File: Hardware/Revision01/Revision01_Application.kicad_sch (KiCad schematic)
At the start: 25 parts, among them J2 Conn_02x08_Odd_Even, J3 Conn_01x04, J4 Conn_02x08_Odd_Even, Q2 PMV32UP,215, Q3 PMV32UP,215, U2 MRF89XAM9AT-I/RM, U4 ICM-45605

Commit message: added back powerflags back for ERC
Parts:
- J2, J4: footprint (none) -> Connector_PinHeader_2.54mm:PinHeader_2x08_P2.54mm_Vertical
- J3: footprint (none) -> Connector_PinHeader_2.54mm:PinHeader_1x04_P2.54mm_Vertical
- U2: footprint MOD_MRF89XAM9A_MCH -> MRF89XAM9AT-antenna:MOD_MRF89XAM9A_MCH
- U4: footprint ICM-45605:XDCR_ICM-45605 -> ICM-45605-gyroscope:XDCR_ICM-45605
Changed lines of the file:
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@@
 			)
 		)
-		(property "Footprint" ""
+		(property "Footprint" "Connector_PinHeader_2.54mm:PinHeader_2x08_P2.54mm_Vertical"
 			(at 127 30.48 0)
 			(effects
@@
 			)
 		)
-		(property "Footprint" ""
+		(property "Footprint" "Connector_PinHeader_2.54mm:PinHeader_2x08_P2.54mm_Vertical"
 			(at 152.4 29.21 0)
 			(effects
@@
 			)
 		)
-		(property "Footprint" ""
+		(property "Footprint" "Connector_PinHeader_2.54mm:PinHeader_1x04_P2.54mm_Vertical"
 			(at 147.32 105.41 0)
 			(effects
@@
 			)
 		)
-		(property "Footprint" "MOD_MRF89XAM9A_MCH"
+		(property "Footprint" "MRF89XAM9AT-antenna:MOD_MRF89XAM9A_MCH"
 			(at 194.31 29.21 0)
 			(effects
@@
 			)
 		)
-		(property "Footprint" "ICM-45605:XDCR_ICM-45605"
+		(property "Footprint" "ICM-45605-gyroscope:XDCR_ICM-45605"
 			(at 231.14 88.9 0)
 			(effects

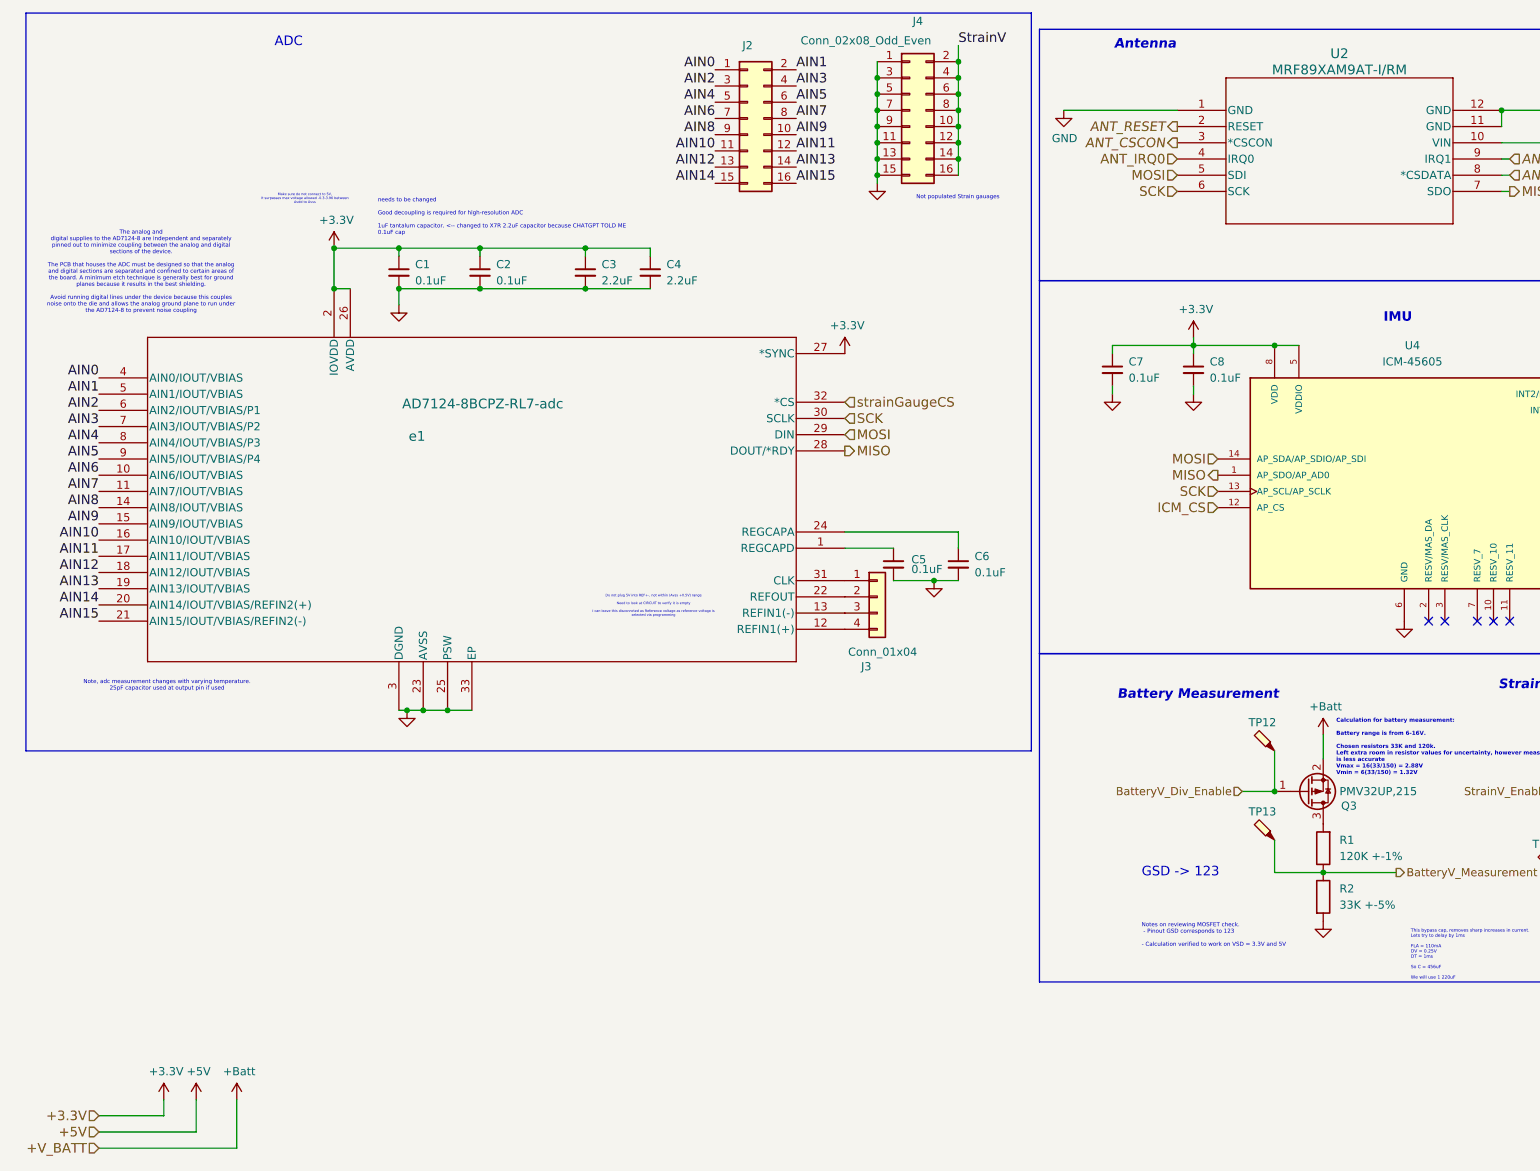
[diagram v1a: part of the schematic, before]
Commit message: added netclasses again changed power to be globally used strain gauges symbol created and added to schematic
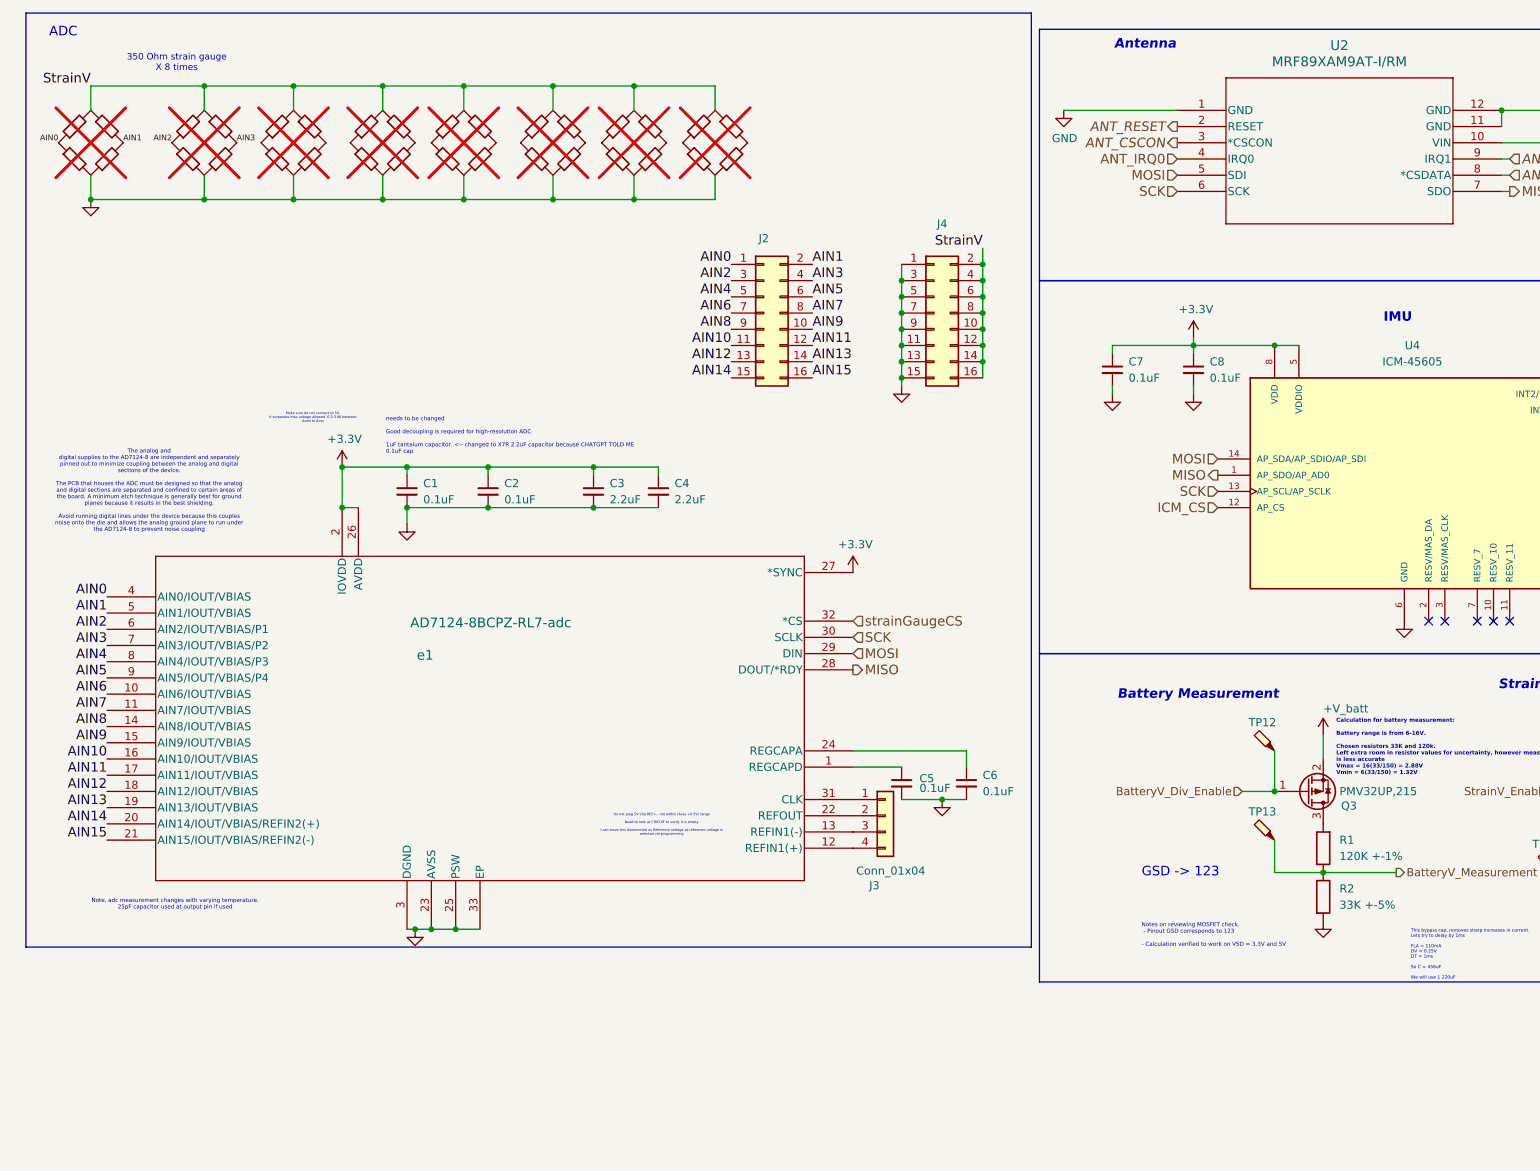
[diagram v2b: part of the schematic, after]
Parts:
- added R18, R3, R4, R5, R6, R7, R8, R9: strainGauge, symbol strainGauge:strainGauge
- J4: value Conn_02x08_Odd_Even -> StrainGaugeMeasurement connector
- U2: Distributor link (none) -> https://www.digikey.ca/en/products/detail/microchip-technol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; Manufacturer Part Number (none) -> 150-MRF89XAM9AT-I/RMDKR-ND
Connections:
- net AIN0: now also R3.1
- net AIN1: now also R3.2
- net AIN2: now also R4.1
- net AIN3: now also R4.2
- net GND: now also R18.1, R3.1, R4.1, R5.1, R6.1, R7.1, R8.1, R9.1
- net StrainV: now also R18.1, R3.1, R4.1, R5.1, R6.1, R7.1, R8.1, R9.1
- net +Batt renamed +V_batt
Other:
- note added: "350 Ohm strain gauge X 8 times"
- note removed: "Not populated Strain gauages"
- moved on the sheet: C1, C2, C3, C4, C5, C6, J2, J3, J4, e1

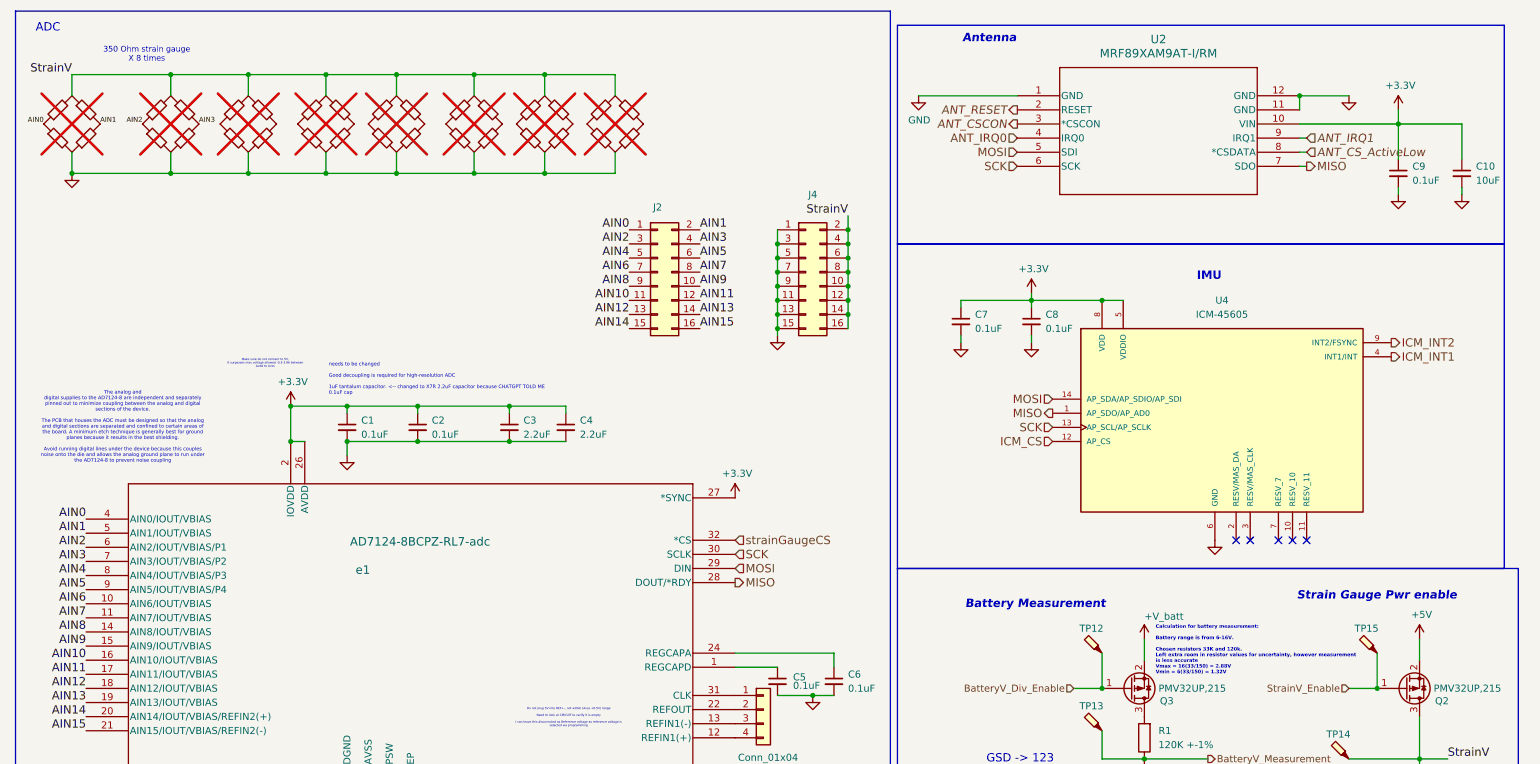
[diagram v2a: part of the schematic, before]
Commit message: added 0ohm resistor to power STRAIN GAUGE. Need to re-read ADC to ensure reference is able to read negative voltage, as well as is capable of reading strain gauge
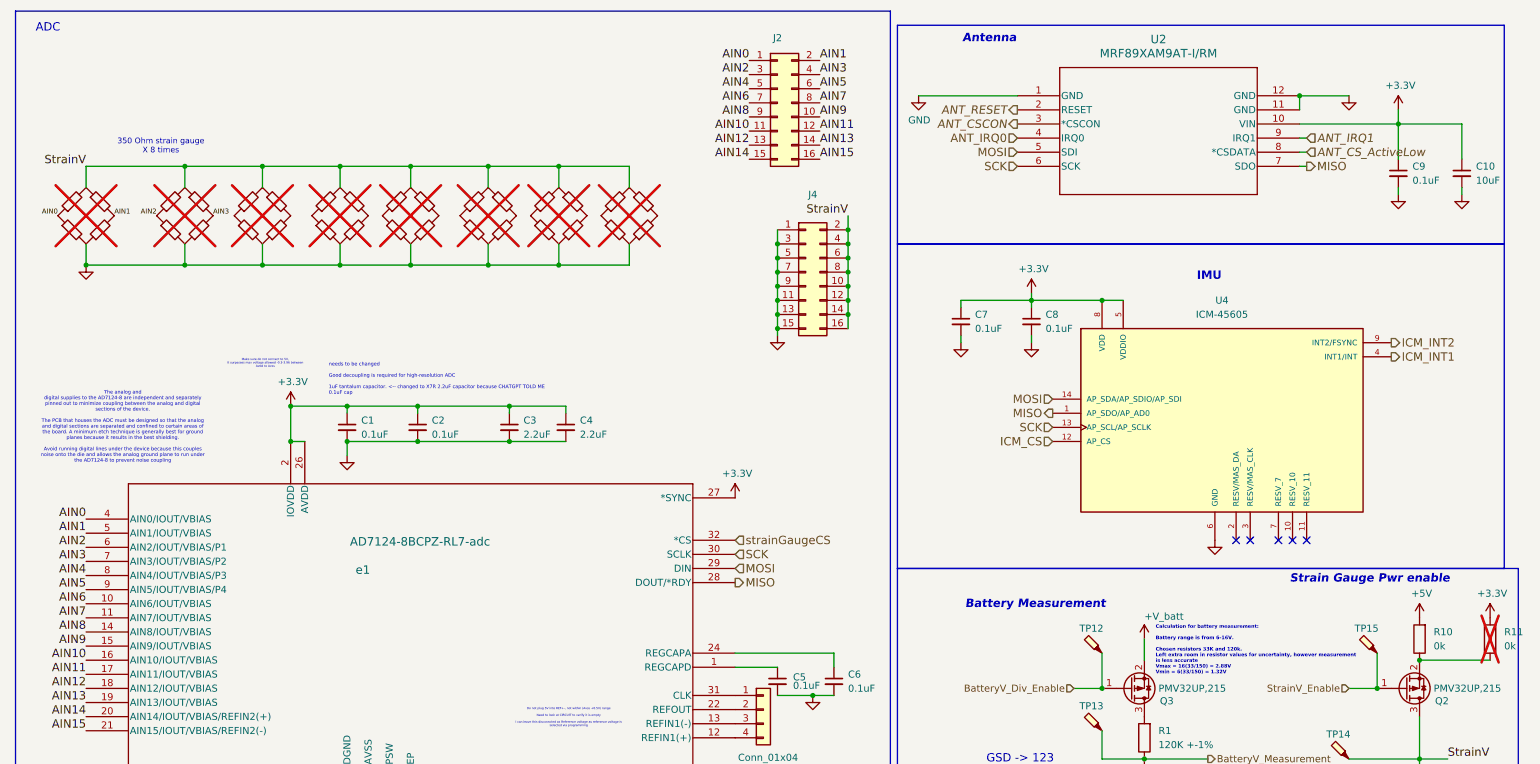
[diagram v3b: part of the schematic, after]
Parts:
- added R10, R11: 0k, symbol Device:R
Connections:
- net +3.3V: now also R11.2
- net +5V: now also R10.2; no longer Q2.2 (S)
- new net: Q2.2 (S), R10.1, R11.1
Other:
- moved on the sheet: J2
